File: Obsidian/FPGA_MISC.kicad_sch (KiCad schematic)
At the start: 21 parts, among them Q3 BSS138LT1G, SW1 SW_DIP_x01, U1 XC7A35T-CSG325, U27 S25FL128SAGMFI001, U9 REF3012

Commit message: update with available components on LCSC
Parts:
- C146, C153: LCSC (none) -> C85926
- C150: LCSC (none) -> C565524
- C151, C152: LCSC (none) -> C76991
- C154: LCSC (none) -> C190187
- L11: LCSC (none) -> C19330
- L15: LCSC (none) -> C383402
- LD5: LCSC (none) -> C5879295
- Q3: FT Rotation Offset (none) -> 180; LCSC (none) -> C82045
- R161: LCSC (none) -> C60490
- R85, R86, R87: LCSC (none) -> C25900
- R88, R89, R90: LCSC (none) -> C11702
- SW1: FT Rotation Offset (none) -> 0; LCSC (none) -> C7421519
- U1: FT Rotation Offset (none) -> 0; LCSC (none) -> C1521749
- U27: FT Rotation Offset (none) -> 270; LCSC (none) -> C111478
- U9: LCSC (none) -> C34674

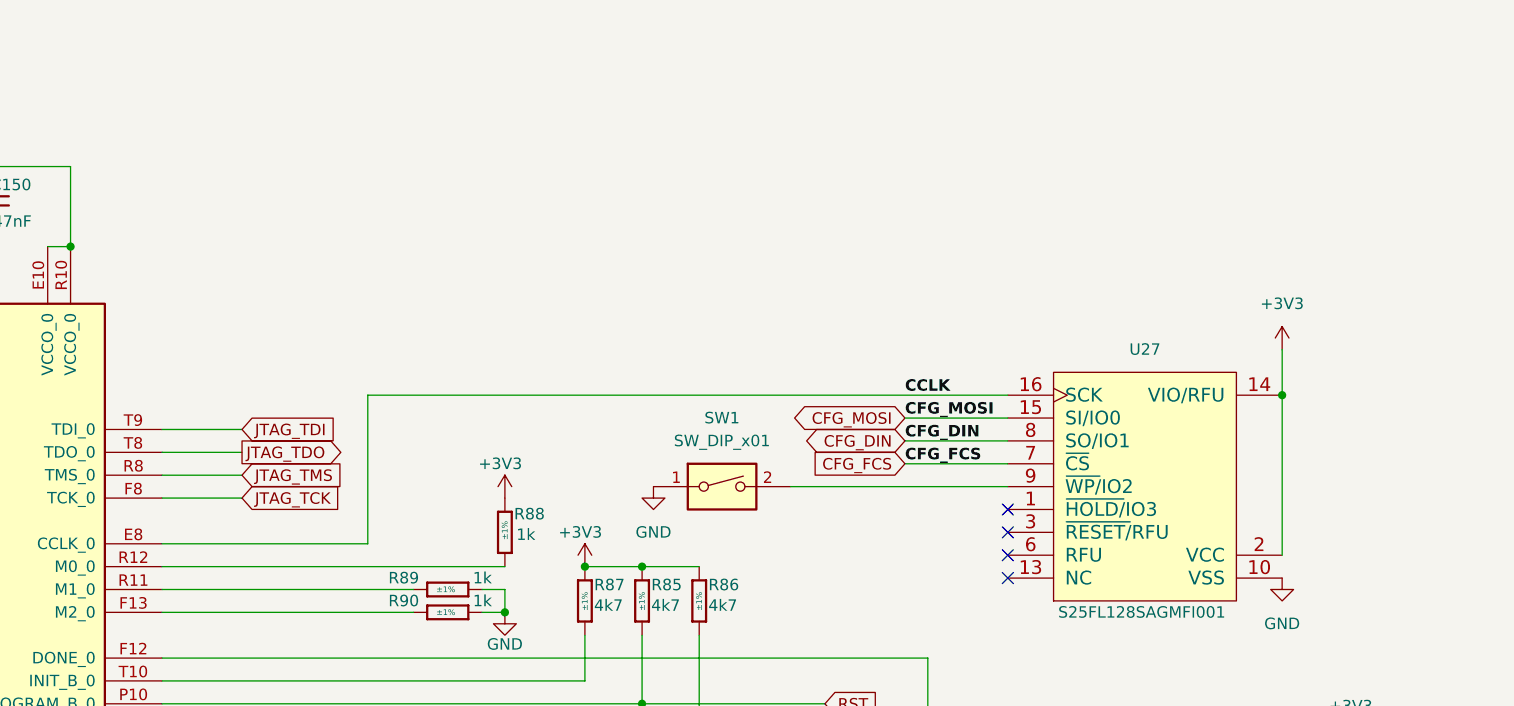
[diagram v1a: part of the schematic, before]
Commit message: replacing global label with hierarchical label
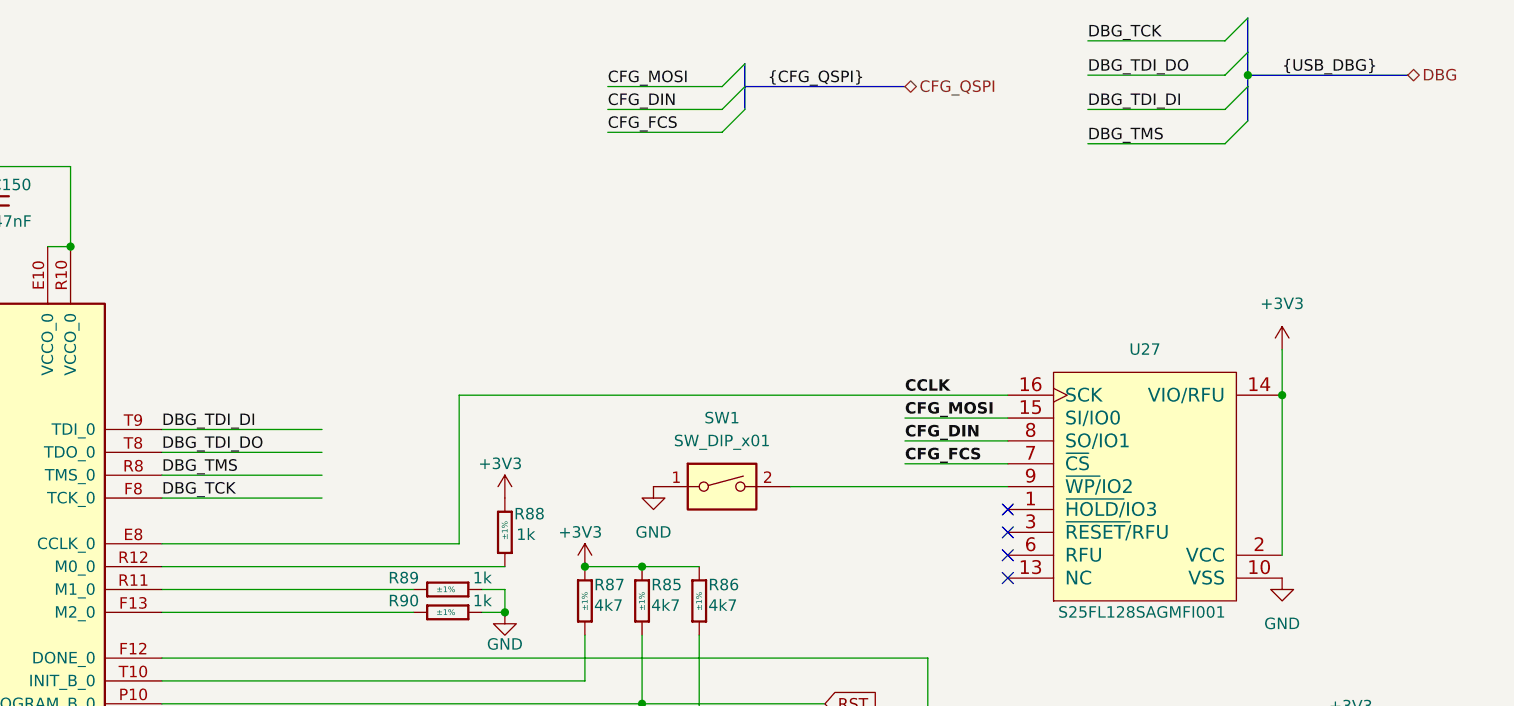
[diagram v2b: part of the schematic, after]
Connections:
- net JTAG_TCK renamed DBG_TCK
- net JTAG_TDI renamed DBG_TDI_DI
- net JTAG_TDO renamed DBG_TDI_DO
- net JTAG_TMS renamed DBG_TMS

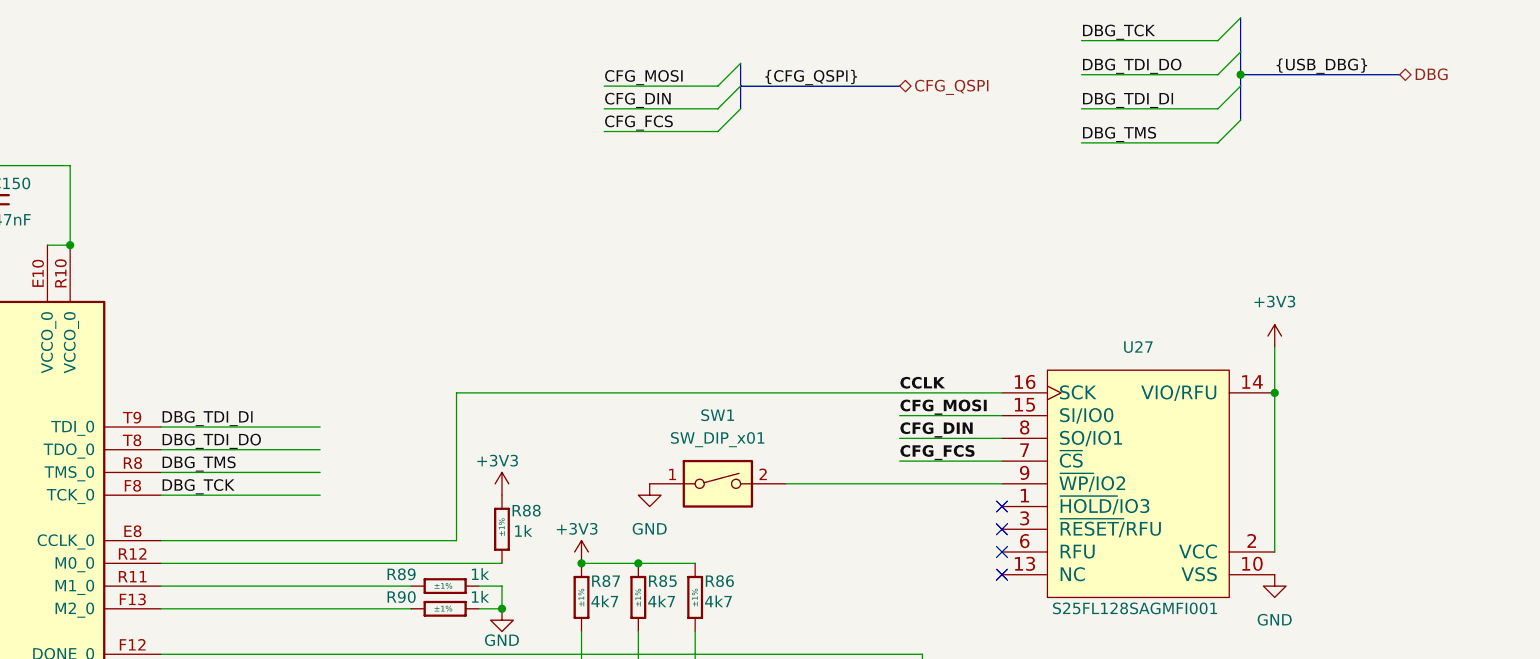
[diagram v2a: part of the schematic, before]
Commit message: Adding symbol library
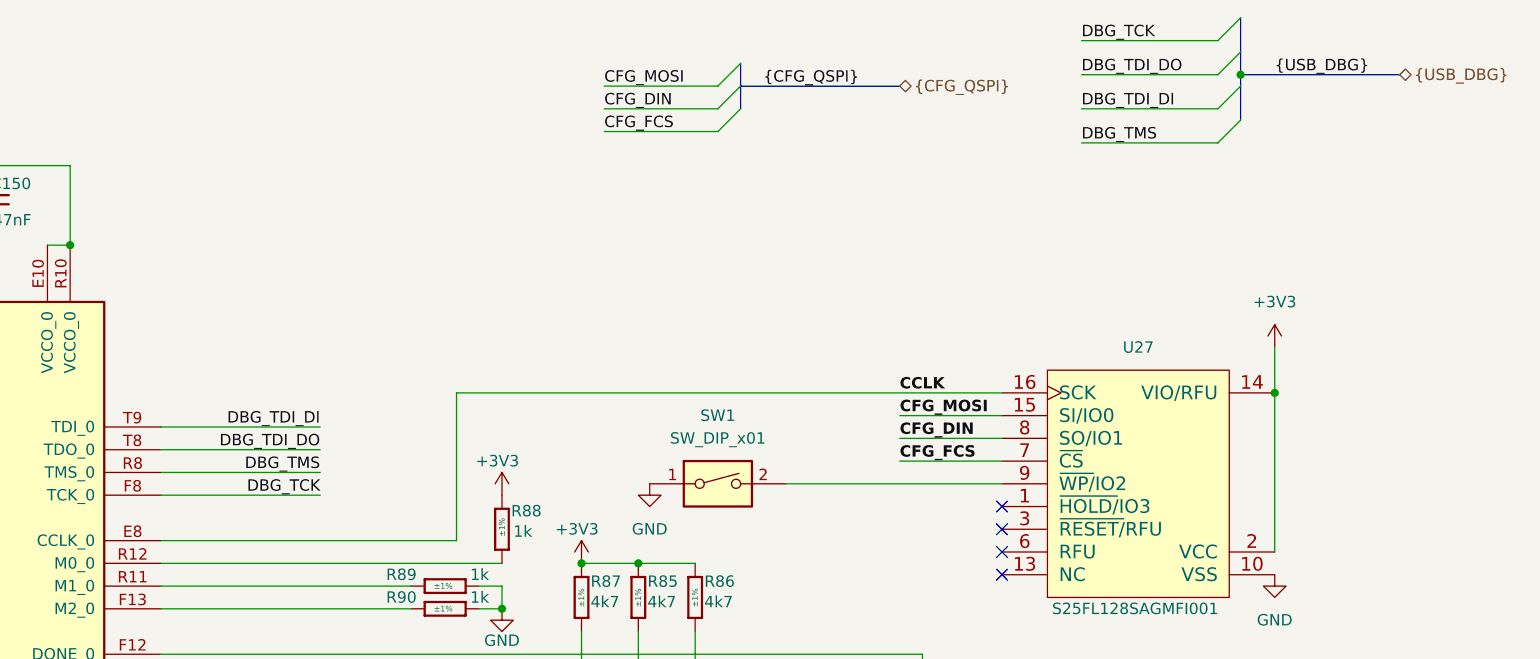
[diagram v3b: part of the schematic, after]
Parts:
- C146, C153: symbol Capacitors SMD:CC0201_470NF_4V_20%_X5R -> Library_Symbol:CC0201_470NF_4V_20%_X5R
- C150: symbol Capacitors SMD:CC0201_47NF_6.3V_10%_X5R -> Library_Symbol:CC0201_47NF_6.3V_10%_X5R
- C151, C152: symbol Capacitors SMD:CC0402_10UF_6.3V_20%_X5R -> Library_Symbol:CC0402_10UF_6.3V_20%_X5R
- C154: symbol Capacitors_SMD:CC0201_100NF_6.3V_10%_X5R -> Library_Symbol:CC0201_100NF_6.3V_10%_X5R
- L11: symbol Inductors SMD:IND0603_MURATA_BLM18AG601SN1 -> Library_Symbol:IND0603_MURATA_BLM18AG601SN1
- L15: symbol Inductors SMD:IND0805_TDK_MLZ2012M150WT000 -> Library_Symbol:IND0805_TDK_MLZ2012M150WT000
- LD5: symbol LEDs & Displays:LED_KINGBRIGHT_KPH-1608CGCK -> Library_Symbol:LED_KINGBRIGHT_KPH-1608CGCK
- Q3: symbol Transistors:BSS138LT1G -> Library_Symbol:BSS138LT1G
- R161: symbol Resistors SMD:R0402_10K_1%_0.0625W_100PPM -> Library_Symbol:R0402_10K_1%_0.0625W_100PPM
- R85, R86, R87: symbol Resistors SMD:R0402_4K7_1%_0.0625W_100PPM -> Library_Symbol:R0402_4K7_1%_0.0625W_100PPM
- R88, R89, R90: symbol Resistors SMD:R0402_1K_1%_0.0625W_100PPM -> Library_Symbol:R0402_1K_1%_0.0625W_100PPM
- SW1: symbol Switch:SW_DIP_x01 -> Library_Symbol:SW_DIP_x01
- U1: symbol FPGA_Xilinx_Artix7:XC7A35T-CSG325 -> Library_Symbol:XC7A35T-CSG325
- U27: symbol Logic:S25FL128SAGMFI001 -> Library_Symbol:S25FL128SAGMFI001
- U9: symbol Reference_Voltage:REF3012 -> Library_Symbol:REF3012
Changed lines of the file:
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@@
 	(wire
 		(pts
-			(xy 121.92 76.2) (xy 139.7 76.2)
+			(xy 160.02 138.43) (xy 167.64 138.43)
 		)
 		(stroke
@@
 	(wire
 		(pts
-			(xy 160.02 138.43) (xy 167.64 138.43)
+			(xy 157.48 130.81) (xy 160.02 130.81)
 		)
 		(stroke
@@
 	(wire
 		(pts
-			(xy 157.48 130.81) (xy 160.02 130.81)
+			(xy 204.47 67.31) (xy 215.9 67.31)
 		)
 		(stroke
@@
 	(wire
 		(pts
-			(xy 204.47 67.31) (xy 215.9 67.31)
+			(xy 171.45 35.56) (xy 184.15 35.56)
 		)
 		(stroke
@@
 	(wire
 		(pts
-			(xy 171.45 35.56) (xy 184.15 35.56)
+			(xy 207.01 124.46) (xy 247.65 124.46)
 		)
 		(stroke
@@
 	(wire
 		(pts
-			(xy 207.01 124.46) (xy 247.65 124.46)
+			(xy 204.47 72.39) (xy 215.9 72.39)
 		)
 		(stroke
@@
 	(wire
 		(pts
-			(xy 204.47 72.39) (xy 215.9 72.39)
+			(xy 162.56 147.32) (xy 167.64 147.32)
 		)
 		(stroke
@@
 	(wire
 		(pts
-			(xy 162.56 147.32) (xy 167.64 147.32)
+			(xy 139.7 68.58) (xy 121.92 68.58)
+		)
+		(stroke
+			(width 0)
+			(type default)
+		)
+	)
+	(wire
+		(pts
+			(xy 139.7 73.66) (xy 121.92 73.66)
 		)
 		(stroke
@@
 	(wire
 		(pts
+			(xy 139.7 76.2) (xy 121.92 76.2)
+		)
+		(stroke
+			(width 0)
+			(type default)
+		)
+	)
+	(wire
+		(pts
 			(xy 111.76 39.37) (xy 111.76 48.26)
 		)
@@
 	(wire
 		(pts
-			(xy 121.92 68.58) (xy 139.7 68.58)
+			(xy 154.94 64.77) (xy 215.9 64.77)
 		)
 		(stroke
@@
 	(wire
 		(pts
-			(xy 154.94 64.77) (xy 215.9 64.77)
+			(xy 139.7 71.12) (xy 121.92 71.12)
 		)
 		(stroke
@@
 	(wire
 		(pts
-			(xy 121.92 71.12) (xy 139.7 71.12)
-		)
-		(stroke
-			(width 0)
-			(type default)
-		)
-	)
-	(wire
-		(pts
 			(xy 129.54 119.38) (xy 133.35 119.38)
 		)
@@
 	(wire
 		(pts
-			(xy 121.92 73.66) (xy 139.7 73.66)
-		)
-		(stroke
-			(width 0)
-			(type default)
-		)
-	)
-	(wire
-		(pts
 			(xy 93.98 39.37) (xy 102.87 39.37)
 		)
@@
 	)
 	(label "DBG_TDI_DI"
-		(at 121.92 68.58 0)
+		(at 139.7 68.58 180)
 		(effects
 			(font
 				(size 1.27 1.27)
 			)
-			(justify left bottom)
+			(justify right bottom)
 		)
 	)
@@
 	)
 	(label "DBG_TCK"
-		(at 121.92 76.2 0)
+		(at 139.7 76.2 180)
 		(effects
 			(font
 				(size 1.27 1.27)
 			)
-			(justify left bottom)
+			(justify right bottom)
 		)
 	)
 	(label "DBG_TDI_DO"
-		(at 121.92 71.12 0)
+		(at 139.7 71.12 180)
 		(effects
 			(font
 				(size 1.27 1.27)
 			)
-			(justify left bottom)
+			(justify right bottom)
 		)
 	)
@@
 	)
 	(label "DBG_TMS"
-		(at 121.92 73.66 0)
+		(at 139.7 73.66 180)
 		(effects
 			(font
 				(size 1.27 1.27)
 			)
-			(justify left bottom)
+			(justify right bottom)
 		)
 	)
@@
 		)
 	)
-	(hierarchical_label "DBG"
+	(hierarchical_label "{USB_DBG}"
 		(shape bidirectional)
 		(at 260.35 29.21 0)
@@
 		)
 	)
-	(hierarchical_label "CFG_QSPI"
+	(hierarchical_label "{CFG_QSPI}"
 		(shape bidirectional)
 		(at 204.47 30.48 0)
@@
 	)
 	(symbol
-		(lib_id "power:+1V0")
+		(lib_id "Library_Symbol:+1V0")
 		(at 146.05 130.81 0)
 		(unit 1)
@@
 	)
 	(symbol
-		(lib_id "Capacitors SMD:CC0402_10UF_6.3V_20%_X5R")
+		(lib_id "Library_Symbol:CC0402_10UF_6.3V_20%_X5R")
 		(at 160.02 138.43 90)
 		(unit 1)
@@
 	)
 	(symbol
-		(lib_id "power:GND")
+		(lib_id "Library_Symbol:GND")
 		(at 121.92 127 0)
 		(unit 1)
@@
 	)
 	(symbol
-		(lib_id "power:GND")
+		(lib_id "Library_Symbol:GND")
 		(at 167.64 147.32 0)
 		(unit 1)
@@
 	)
 	(symbol
-		(lib_id "power:GND")
+		(lib_id "Library_Symbol:GND")
 		(at 200.66 146.05 0)
 		(unit 1)
@@
 	)
 	(symbol
-		(lib_id "Reference_Voltage:REF3012")
+		(lib_id "Library_Symbol:REF3012")
 		(at 189.23 138.43 0)
 		(unit 1)
@@
 	)
 	(symbol
-		(lib_id "Capacitors SMD:CC0201_470NF_4V_20%_X5R")
+		(lib_id "Library_Symbol:CC0201_470NF_4V_20%_X5R")
 		(at 167.64 138.43 90)
 		(unit 1)
@@
 	)
 	(symbol
-		(lib_id "Capacitors SMD:CC0201_470NF_4V_20%_X5R")
+		(lib_id "Library_Symbol:CC0201_470NF_4V_20%_X5R")
 		(at 93.98 46.99 90)
 		(unit 1)
@@
 	)
 	(symbol
-		(lib_id "FPGA_Xilinx_Artix7:XC7A35T-CSG325")
+		(lib_id "Library_Symbol:XC7A35T-CSG325")
 		(at 83.82 88.9 0)
 		(unit 5)
@@
 	)
 	(symbol
-		(lib_id "Capacitors_SMD:CC0201_100NF_6.3V_10%_X5R")
+		(lib_id "Library_Symbol:CC0201_100NF_6.3V_10%_X5R")
 		(at 133.35 119.38 0)
 		(unit 1)
@@
 	)
 	(symbol
-		(lib_id "power:+1V0")
+		(lib_id "Library_Symbol:+1V0")
 		(at 160.02 76.2 0)
 		(unit 1)
@@
 	)
 	(symbol
-		(lib_id "Capacitors SMD:CC0402_10UF_6.3V_20%_X5R")
+		(lib_id "Library_Symbol:CC0402_10UF_6.3V_20%_X5R")
 		(at 200.66 146.05 90)
 		(unit 1)
@@
 	)
 	(symbol
-		(lib_id "Inductors SMD:IND0603_MURATA_BLM18AG601SN1")
+		(lib_id "Library_Symbol:IND0603_MURATA_BLM18AG601SN1")
 		(at 154.94 147.32 0)
 		(unit 1)
@@
 	)
 	(symbol
-		(lib_id "power:+1V0")
+		(lib_id "Library_Symbol:+1V0")
 		(at 93.98 39.37 0)
 		(unit 1)
@@
 	)
 	(symbol
-		(lib_id "Switch:SW_DIP_x01")
+		(lib_id "Library_Symbol:SW_DIP_x01")
 		(at 184.15 74.93 0)
 		(unit 1)
@@
 	)
 	(symbol
-		(lib_id "power:GND")
+		(lib_id "Library_Symbol:GND")
 		(at 160.02 138.43 0)
 		(unit 1)
@@
 	)
 	(symbol
-		(lib_id "Resistors SMD:R0402_10K_1%_0.0625W_100PPM")
+		(lib_id "Library_Symbol:R0402_10K_1%_0.0625W_100PPM")
 		(at 254 110.49 90)
 		(unit 1)
@@
 	)
 	(symbol
-		(lib_id "power:GND")
+		(lib_id "Library_Symbol:GND")
 		(at 254 128.27 0)
 		(unit 1)
@@
 	)
 	(symbol
-		(lib_id "Capacitors SMD:CC0201_47NF_6.3V_10%_X5R")
+		(lib_id "Library_Symbol:CC0201_47NF_6.3V_10%_X5R")
 		(at 102.87 46.99 90)
 		(unit 1)
@@
 	)
 	(symbol
-		(lib_id "Transistors:BSS138LT1G")
+		(lib_id "Library_Symbol:BSS138LT1G")
 		(at 247.65 124.46 0)
 		(unit 1)
@@
 	)
 	(symbol
-		(lib_id "Resistors SMD:R0402_1K_1%_0.0625W_100PPM")
+		(lib_id "Library_Symbol:R0402_1K_1%_0.0625W_100PPM")
 		(at 160.02 83.82 90)
 		(unit 1)
@@
 	)
 	(symbol
-		(lib_id "power:GND")
+		(lib_id "Library_Symbol:GND")
 		(at 129.54 119.38 0)
 		(unit 1)
@@
 	)
 	(symbol
-		(lib_id "Logic:S25FL128SAGMFI001")
+		(lib_id "Library_Symbol:S25FL128SAGMFI001")
 		(at 220.98 62.23 0)
 		(unit 1)
@@
 	)
 	(symbol
-		(lib_id "power:GND")
+		(lib_id "Library_Symbol:GND")
 		(at 93.98 46.99 0)
 		(unit 1)
@@
 	)
 	(symbol
-		(lib_id "Resistors SMD:R0402_1K_1%_0.0625W_100PPM")
+		(lib_id "Library_Symbol:R0402_1K_1%_0.0625W_100PPM")
 		(at 157.48 88.9 180)
 		(unit 1)
@@
 	)
 	(symbol
-		(lib_id "power:+1V0")
+		(lib_id "Library_Symbol:+1V0")
 		(at 168.91 83.82 0)
 		(unit 1)
@@
 	)
 	(symbol
-		(lib_id "Resistors SMD:R0402_1K_1%_0.0625W_100PPM")
+		(lib_id "Library_Symbol:R0402_1K_1%_0.0625W_100PPM")
 		(at 157.48 86.36 180)
 		(unit 1)
@@
 	)
 	(symbol
-		(lib_id "power:GND")
+		(lib_id "Library_Symbol:GND")
 		(at 186.69 146.05 0)
 		(unit 1)
@@
 	)
 	(symbol
-		(lib_id "power:GND")
+		(lib_id "Library_Symbol:GND")
 		(at 146.05 147.32 0)
 		(unit 1)
@@
 	)
 	(symbol
-		(lib_id "Resistors SMD:R0402_4K7_1%_0.0625W_100PPM")
+		(lib_id "Library_Symbol:R0402_4K7_1%_0.0625W_100PPM")
 		(at 181.61 91.44 90)
 		(unit 1)
@@
 	)
 	(symbol
-		(lib_id "Resistors SMD:R0402_4K7_1%_0.0625W_100PPM")
+		(lib_id "Library_Symbol:R0402_4K7_1%_0.0625W_100PPM")
 		(at 168.91 91.44 90)
 		(unit 1)
@@
 	)
 	(symbol
-		(lib_id "power:GND")
+		(lib_id "Library_Symbol:GND")
 		(at 160.02 88.9 0)
 		(unit 1)
@@
 	)
 	(symbol
-		(lib_id "power:GND")
+		(lib_id "Library_Symbol:GND")
 		(at 246.38 85.09 0)
 		(unit 1)
@@
 	)
 	(symbol
-		(lib_id "Resistors SMD:R0402_4K7_1%_0.0625W_100PPM")
+		(lib_id "Library_Symbol:R0402_4K7_1%_0.0625W_100PPM")
 		(at 175.26 91.44 90)
 		(unit 1)
@@
 	)
 	(symbol
-		(lib_id "LEDs & Displays:LED_KINGBRIGHT_KPH-1608CGCK")
+		(lib_id "Library_Symbol:LED_KINGBRIGHT_KPH-1608CGCK")
 		(at 254 114.3 270)
 		(unit 1)
@@
 	)
 	(symbol
-		(lib_id "power:GND")
+		(lib_id "Library_Symbol:GND")
 		(at 127 111.76 0)
 		(unit 1)
@@
 	)
 	(symbol
-		(lib_id "power:GND")
+		(lib_id "Library_Symbol:GND")
 		(at 176.53 74.93 0)
 		(unit 1)
@@
 	)
 	(symbol
-		(lib_id "power:+1V0")
+		(lib_id "Library_Symbol:+1V0")
 		(at 246.38 59.69 0)
 		(unit 1)
@@
 	)
 	(symbol
-		(lib_id "power:+1V0")
+		(lib_id "Library_Symbol:+1V0")
 		(at 254 102.87 0)
 		(unit 1)
@@
 	)
 	(symbol
-		(lib_id "Inductors SMD:IND0805_TDK_MLZ2012M150WT000")
+		(lib_id "Library_Symbol:IND0805_TDK_MLZ2012M150WT000")
 		(at 149.86 130.81 0)
 		(unit 1)
